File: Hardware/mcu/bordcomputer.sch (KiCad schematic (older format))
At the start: 0 parts

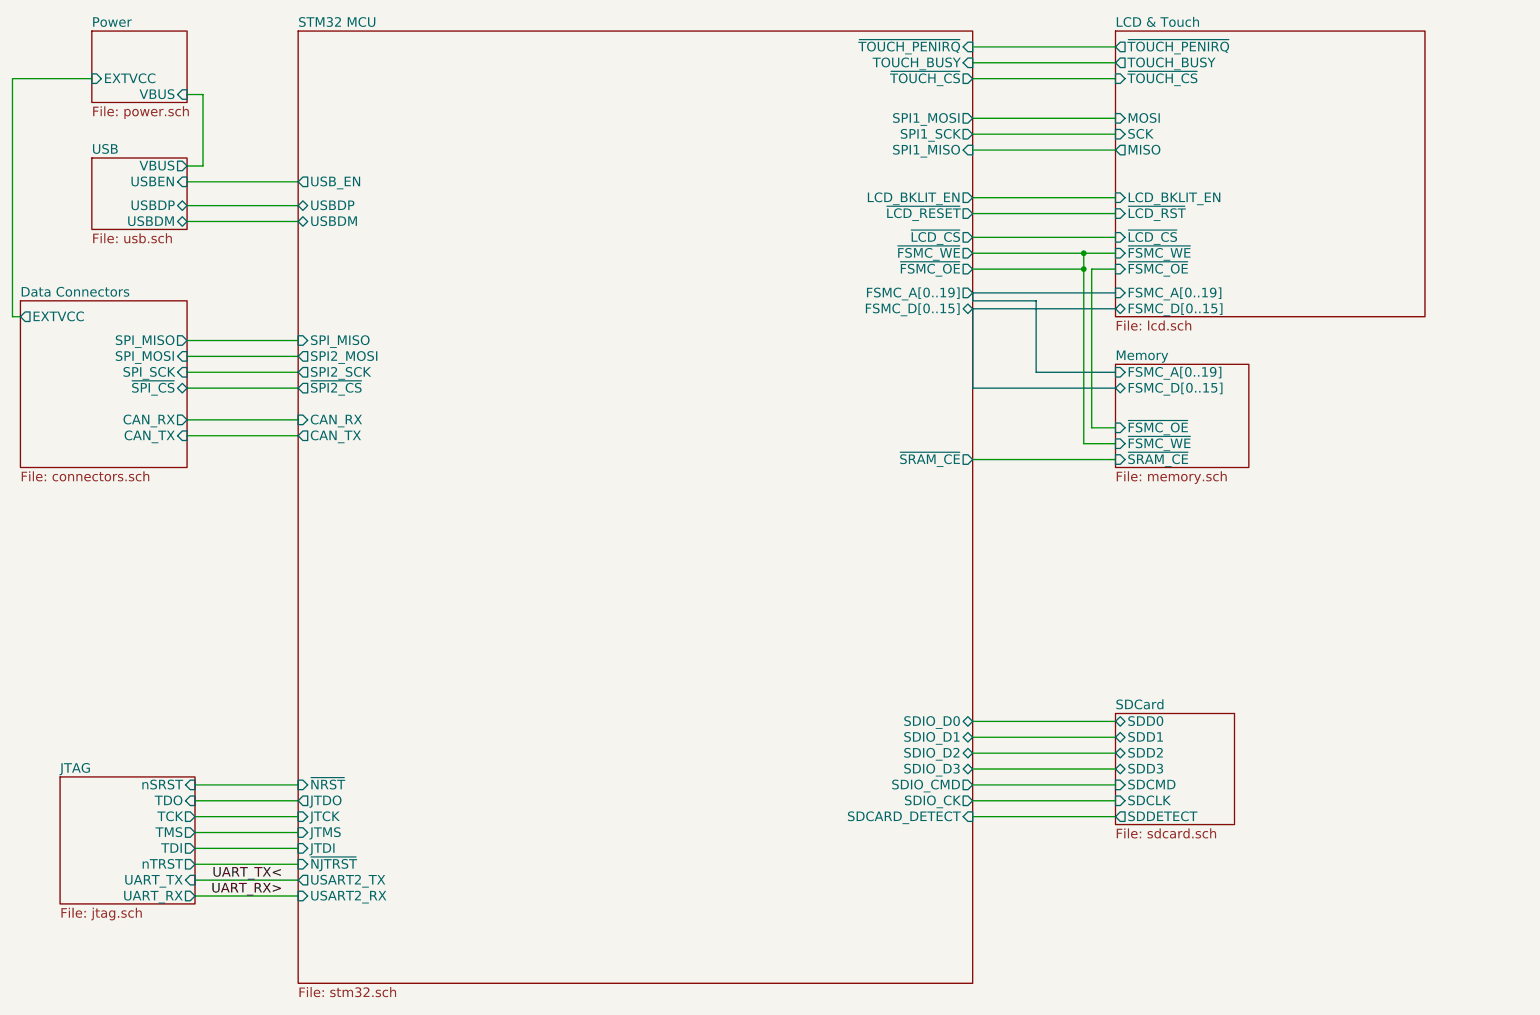
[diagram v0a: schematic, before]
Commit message: splitted schematics are ready. MCU/Display board is ready.
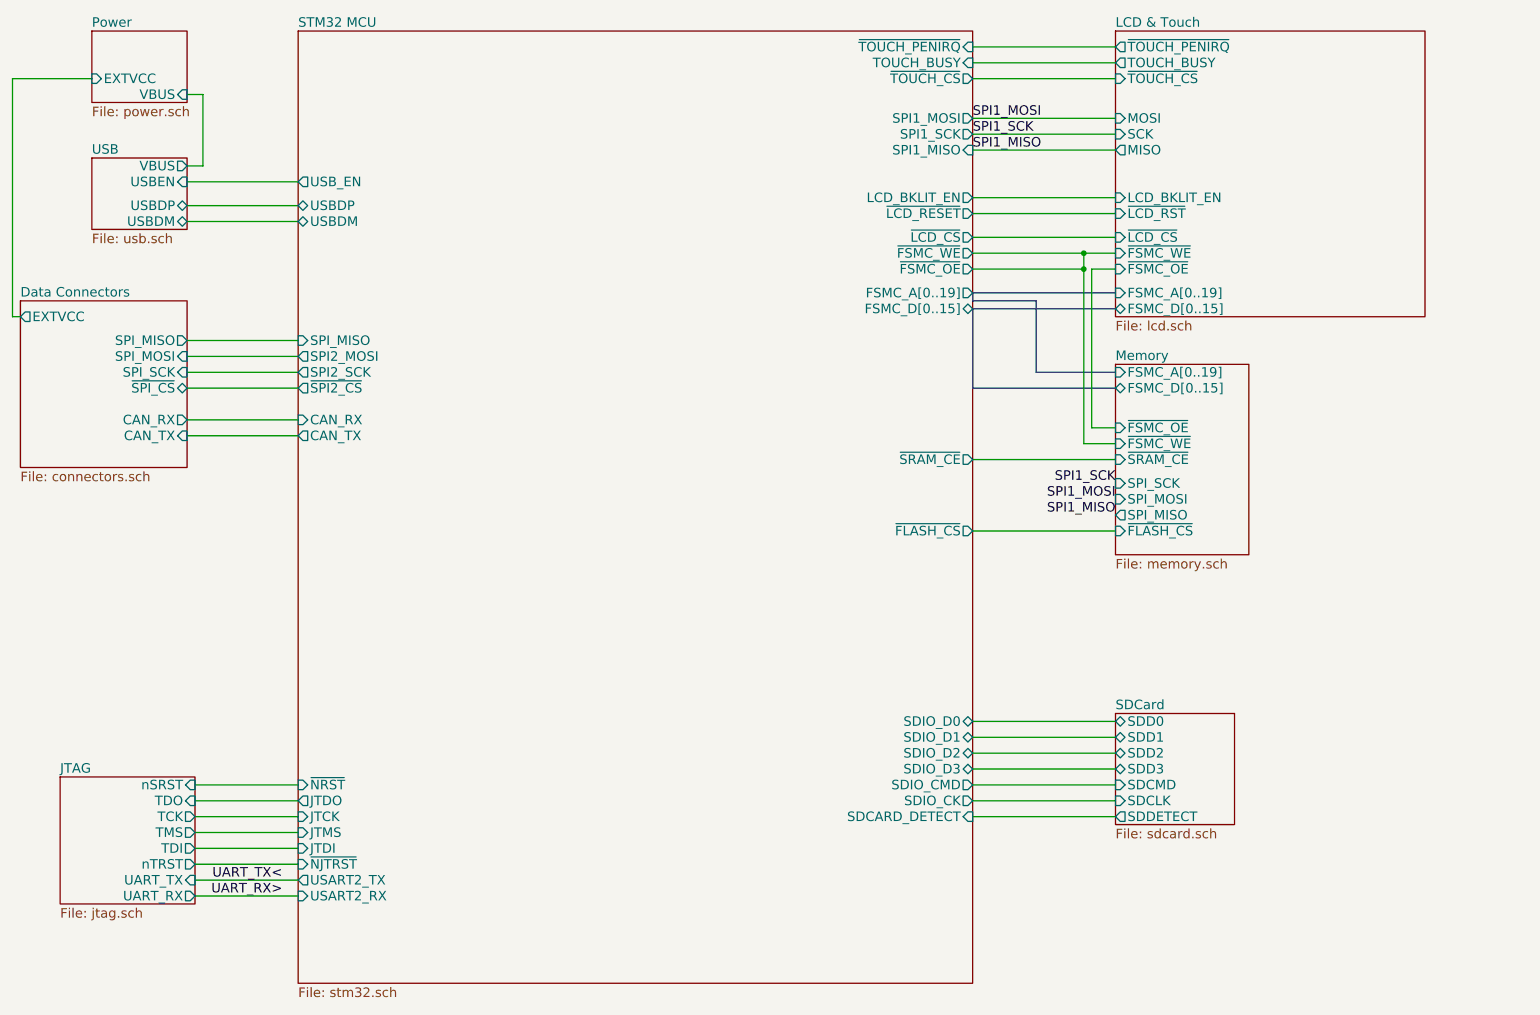
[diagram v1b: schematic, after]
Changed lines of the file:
@@
-EESchema Schematic File Version 2  date Do 10 Mär 2011 01:37:58 CET
+EESchema Schematic File Version 2  date Do 10 Mär 2011 16:44:23 CET
 LIBS:power
 LIBS:device
@@
 EELAYER END
 $Descr A4 11700 8267
+encoding utf-8
 Sheet 1 9
 Title ""
-Date "9 mar 2011"
+Date "10 mar 2011"
 Rev ""
 Comp ""
@@
 $EndDescr
 Wire Wire Line
+	8100 4350 7200 4350
+Wire Wire Line
+	2950 3750 2250 3750
+Wire Wire Line
+	1650 1500 1150 1500
+Wire Wire Line
+	1150 1500 1150 3000
+Wire Wire Line
+	1150 3000 1200 3000
+Wire Bus Line
+	7600 2900 7600 3350
+Wire Bus Line
+	7600 2900 7200 2900
+Wire Bus Line
+	7200 2900 7200 2850
+Wire Bus Line
+	8100 2950 7200 2950
+Wire Bus Line
+	7600 3350 8100 3350
+Wire Wire Line
+	7200 1500 8100 1500
+Wire Wire Line
+	7200 1400 8100 1400
+Wire Wire Line
+	7200 1300 8100 1300
+Wire Wire Line
+	2300 6650 2950 6650
+Wire Wire Line
+	2300 6550 2950 6550
+Wire Wire Line
+	2300 6450 2950 6450
+Wire Wire Line
+	2300 6350 2950 6350
+Wire Wire Line
+	2300 6250 2950 6250
+Wire Wire Line
+	2300 6150 2950 6150
+Wire Wire Line
+	2300 6050 2950 6050
+Wire Wire Line
+	2300 5950 2950 5950
+Wire Wire Line
+	2950 2400 2250 2400
+Wire Wire Line
+	2950 2300 2250 2300
+Wire Wire Line
+	7200 3900 8100 3900
+Connection ~ 7900 2600
+Wire Wire Line
+	7200 2600 8100 2600
+Wire Wire Line
+	8100 3800 7900 3800
+Wire Wire Line
+	7900 3800 7900 2600
+Wire Wire Line
+	2250 2050 2350 2050
+Wire Wire Line
+	2350 2050 2350 1600
+Wire Wire Line
+	2350 1600 2250 1600
+Wire Wire Line
+	8100 2700 7950 2700
+Wire Wire Line
+	7950 2700 7950 3700
+Wire Wire Line
+	7950 3700 8100 3700
+Wire Wire Line
+	7200 2500 8100 2500
+Wire Wire Line
+	7200 2700 7900 2700
+Connection ~ 7900 2700
+Wire Bus Line
+	7200 2850 8100 2850
+Wire Wire Line
+	2250 2150 2950 2150
+Wire Wire Line
+	8100 5550 7200 5550
+Wire Wire Line
+	8100 5650 7200 5650
+Wire Wire Line
+	8100 5750 7200 5750
+Wire Wire Line
+	8100 5850 7200 5850
+Wire Wire Line
+	8100 5950 7200 5950
+Wire Wire Line
+	8100 6050 7200 6050
+Wire Wire Line
+	8100 6150 7200 6150
+Wire Wire Line
+	7200 2250 8100 2250
+Wire Wire Line
+	7200 2350 8100 2350
+Wire Bus Line
+	7200 2950 7200 3450
+Wire Bus Line
+	7200 3450 8100 3450
+Wire Wire Line
+	7200 1750 8100 1750
+Wire Wire Line
+	7200 1850 8100 1850
+Wire Wire Line
+	7200 1950 8100 1950
+Wire Wire Line
+	2250 3650 2950 3650
+Wire Wire Line
+	2250 3150 2950 3150
+Wire Wire Line
+	2250 3250 2950 3250
+Wire Wire Line
+	2250 3350 2950 3350
+Wire Wire Line
 	2250 3450 2950 3450
-Wire Wire Line
-	2250 3350 2950 3350
-Wire Wire Line
-	2250 3250 2950 3250
-Wire Wire Line
-	2250 3150 2950 3150
-Wire Wire Line
-	2250 3650 2950 3650
-Wire Wire Line
-	7200 1950 8100 1950
-Wire Wire Line
-	7200 1850 8100 1850
-Wire Wire Line
-	7200 1750 8100 1750
-Wire Bus Line
-	8100 3450 7200 3450
-Wire Bus Line
-	7200 3450 7200 2950
-Wire Wire Line
-	7200 2350 8100 2350
-Wire Wire Line
-	7200 2250 8100 2250
-Wire Wire Line
-	8100 6150 7200 6150
-Wire Wire Line
-	8100 6050 7200 6050
-Wire Wire Line
-	8100 5950 7200 5950
-Wire Wire Line
-	8100 5850 7200 5850
-Wire Wire Line
-	8100 5750 7200 5750
-Wire Wire Line
-	8100 5650 7200 5650
-Wire Wire Line
-	8100 5550 7200 5550
-Wire Wire Line
-	2250 2150 2950 2150
-Wire Bus Line
-	8100 2850 7200 2850
-Connection ~ 7900 2700
-Wire Wire Line
-	7200 2700 7900 2700
-Wire Wire Line
-	7200 2500 8100 2500
-Wire Wire Line
-	8100 3700 7950 3700
-Wire Wire Line
-	7950 3700 7950 2700
-Wire Wire Line
-	7950 2700 8100 2700
-Wire Wire Line
-	2250 1600 2350 1600
-Wire Wire Line
-	2350 1600 2350 2050
-Wire Wire Line
-	2350 2050 2250 2050
-Wire Wire Line
-	7900 2600 7900 3800
-Wire Wire Line
-	7900 3800 8100 3800
-Wire Wire Line
-	7200 2600 8100 2600
-Connection ~ 7900 2600
-Wire Wire Line
-	7200 3900 8100 3900
-Wire Wire Line
-	2950 2300 2250 2300
-Wire Wire Line
-	2950 2400 2250 2400
-Wire Wire Line
-	2300 5950 2950 5950
-Wire Wire Line
-	2300 6050 2950 6050
-Wire Wire Line
-	2300 6150 2950 6150
-Wire Wire Line
-	2300 6250 2950 6250
-Wire Wire Line
-	2300 6350 2950 6350
-Wire Wire Line
-	2300 6450 2950 6450
-Wire Wire Line
-	2300 6550 2950 6550
-Wire Wire Line
-	2300 6650 2950 6650
-Wire Wire Line
-	7200 1300 8100 1300
-Wire Wire Line
-	7200 1400 8100 1400
-Wire Wire Line
-	7200 1500 8100 1500
-Wire Bus Line
-	8100 3350 7600 3350
-Wire Bus Line
-	7200 2950 8100 2950
-Wire Bus Line
-	7200 2850 7200 2900
-Wire Bus Line
-	7200 2900 7600 2900
-Wire Bus Line
-	7600 2900 7600 3350
-Wire Wire Line
-	1200 3000 1150 3000
-Wire Wire Line
-	1150 3000 1150 1500
-Wire Wire Line
-	1150 1500 1650 1500
-Wire Wire Line
-	2950 3750 2250 3750
+Text Label 8100 4250 2    60   ~ 0
+SPI1_MISO
+Text Label 8100 4150 2    60   ~ 0
+SPI1_MOSI
+Text Label 8100 4050 2    60   ~ 0
+SPI1_SCK
+Text Label 7200 1850 0    60   ~ 0
+SPI1_SCK
+Text Label 7200 1950 0    60   ~ 0
+SPI1_MISO
+Text Label 7200 1750 0    60   ~ 0
+SPI1_MOSI
 $Sheet
 S 1200 2900 1050 1050
@@
 $EndSheet
 $Sheet
-S 8100 3300 840  650
+S 8100 3300 840  1200
 U 4D74466C
 F0 "Memory" 60
@@
 F5 "FSMC_D[0..15]" B L 8100 3450 60
 F6 "FSMC_A[0..19]" I L 8100 3350 60
+F7 "SPI_SCK" I L 8100 4050 60
+F8 "SPI_MOSI" I L 8100 4150 60
+F9 "SPI_MISO" O L 8100 4250 60
+F10 "~FLASH_CS" I L 8100 4350 60
 $EndSheet
 $Sheet
@@
 F38 "SPI2_SCK" O L 2950 3350 60
 F39 "~SPI2_CS" O L 2950 3450 60
+F40 "~FLASH_CS" O R 7200 4350 60
 $EndSheet
 $EndSCHEMATC

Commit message: mounting holes and test version of the bottom of the housing for the sensors pcb
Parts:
- added P101, P102, P103, P104: CONN_1, symbol CONN_1
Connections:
- new net GND: P101.1, P102.1, P103.1, P104.1
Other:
- note added: "Mounting holes"
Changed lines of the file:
@@
-EESchema Schematic File Version 2  date Do 10 Mär 2011 16:44:23 CET
+EESchema Schematic File Version 2  date Mo 21 Mär 2011 03:16:23 CET
 LIBS:power
 LIBS:device
@@
 Sheet 1 9
 Title ""
-Date "10 mar 2011"
+Date "21 mar 2011"
 Rev ""
 Comp ""
@@
 Comment4 ""
 $EndDescr
+Wire Notes Line
+	9850 6500 10550 6500
+Wire Notes Line
+	9850 6500 9850 6950
+Wire Notes Line
+	9850 6950 10550 6950
+Wire Notes Line
+	10550 6950 10550 6500
+Connection ~ 10300 6700
+Wire Wire Line
+	10400 6600 10300 6600
+Wire Wire Line
+	2250 3450 2950 3450
+Wire Wire Line
+	2250 3350 2950 3350
+Wire Wire Line
+	2250 3250 2950 3250
+Wire Wire Line
+	2250 3150 2950 3150
+Wire Wire Line
+	2250 3650 2950 3650
+Wire Wire Line
+	7200 1950 8100 1950
+Wire Wire Line
+	7200 1850 8100 1850
+Wire Wire Line
+	7200 1750 8100 1750
+Wire Bus Line
+	8100 3450 7200 3450
+Wire Bus Line
+	7200 3450 7200 2950
+Wire Wire Line
+	7200 2350 8100 2350
+Wire Wire Line
+	7200 2250 8100 2250
+Wire Wire Line
+	8100 6150 7200 6150
+Wire Wire Line
+	8100 6050 7200 6050
+Wire Wire Line
+	8100 5950 7200 5950
+Wire Wire Line
+	8100 5850 7200 5850
+Wire Wire Line
+	8100 5750 7200 5750
+Wire Wire Line
+	8100 5650 7200 5650
+Wire Wire Line
+	8100 5550 7200 5550
+Wire Wire Line
+	2250 2150 2950 2150
+Wire Bus Line
+	8100 2850 7200 2850
+Connection ~ 7900 2700
+Wire Wire Line
+	7200 2700 7900 2700
+Wire Wire Line
+	7200 2500 8100 2500
+Wire Wire Line
+	8100 3700 7950 3700
+Wire Wire Line
+	7950 3700 7950 2700
+Wire Wire Line
+	7950 2700 8100 2700
+Wire Wire Line
+	2250 1600 2350 1600
+Wire Wire Line
+	2350 1600 2350 2050
+Wire Wire Line
+	2350 2050 2250 2050
+Wire Wire Line
+	7900 2600 7900 3800
+Wire Wire Line
+	7900 3800 8100 3800
+Wire Wire Line
+	7200 2600 8100 2600
+Connection ~ 7900 2600
+Wire Wire Line
+	7200 3900 8100 3900
+Wire Wire Line
+	2950 2300 2250 2300
+Wire Wire Line
+	2950 2400 2250 2400
+Wire Wire Line
+	2300 5950 2950 5950
+Wire Wire Line
+	2300 6050 2950 6050
+Wire Wire Line
+	2300 6150 2950 6150
+Wire Wire Line
+	2300 6250 2950 6250
+Wire Wire Line
+	2300 6350 2950 6350
+Wire Wire Line
+	2300 6450 2950 6450
+Wire Wire Line
+	2300 6550 2950 6550
+Wire Wire Line
+	2300 6650 2950 6650
+Wire Wire Line
+	7200 1300 8100 1300
+Wire Wire Line
+	7200 1400 8100 1400
+Wire Wire Line
+	7200 1500 8100 1500
+Wire Bus Line
+	8100 3350 7600 3350
+Wire Bus Line
+	7200 2950 8100 2950
+Wire Bus Line
+	7200 2850 7200 2900
+Wire Bus Line
+	7200 2900 7600 2900
+Wire Bus Line
+	7600 2900 7600 3350
+Wire Wire Line
+	1200 3000 1150 3000
+Wire Wire Line
+	1150 3000 1150 1500
+Wire Wire Line
+	1150 1500 1650 1500
+Wire Wire Line
+	2950 3750 2250 3750
 Wire Wire Line
 	8100 4350 7200 4350
 Wire Wire Line
-	2950 3750 2250 3750
-Wire Wire Line
-	1650 1500 1150 1500
-Wire Wire Line
-	1150 1500 1150 3000
-Wire Wire Line
-	1150 3000 1200 3000
-Wire Bus Line
-	7600 2900 7600 3350
-Wire Bus Line
-	7600 2900 7200 2900
-Wire Bus Line
-	7200 2900 7200 2850
-Wire Bus Line
-	8100 2950 7200 2950
-Wire Bus Line
-	7600 3350 8100 3350
-Wire Wire Line
-	7200 1500 8100 1500
-Wire Wire Line
-	7200 1400 8100 1400
-Wire Wire Line
-	7200 1300 8100 1300
-Wire Wire Line
-	2300 6650 2950 6650
-Wire Wire Line
-	2300 6550 2950 6550
-Wire Wire Line
-	2300 6450 2950 6450
-Wire Wire Line
-	2300 6350 2950 6350
-Wire Wire Line
-	2300 6250 2950 6250
-Wire Wire Line
-	2300 6150 2950 6150
-Wire Wire Line
-	2300 6050 2950 6050
-Wire Wire Line
-	2300 5950 2950 5950
-Wire Wire Line
-	2950 2400 2250 2400
-Wire Wire Line
-	2950 2300 2250 2300
-Wire Wire Line
-	7200 3900 8100 3900
-Connection ~ 7900 2600
-Wire Wire Line
-	7200 2600 8100 2600
-Wire Wire Line
-	8100 3800 7900 3800
-Wire Wire Line
-	7900 3800 7900 2600
-Wire Wire Line
-	2250 2050 2350 2050
-Wire Wire Line
-	2350 2050 2350 1600
-Wire Wire Line
-	2350 1600 2250 1600
-Wire Wire Line
-	8100 2700 7950 2700
-Wire Wire Line
-	7950 2700 7950 3700
-Wire Wire Line
-	7950 3700 8100 3700
-Wire Wire Line
-	7200 2500 8100 2500
-Wire Wire Line
-	7200 2700 7900 2700
-Connection ~ 7900 2700
-Wire Bus Line
-	7200 2850 8100 2850
-Wire Wire Line
-	2250 2150 2950 2150
-Wire Wire Line
-	8100 5550 7200 5550
-Wire Wire Line
-	8100 5650 7200 5650
-Wire Wire Line
-	8100 5750 7200 5750
-Wire Wire Line
-	8100 5850 7200 5850
-Wire Wire Line
-	8100 5950 7200 5950
-Wire Wire Line
-	8100 6050 7200 6050
-Wire Wire Line
-	8100 6150 7200 6150
-Wire Wire Line
-	7200 2250 8100 2250
-Wire Wire Line
-	7200 2350 8100 2350
-Wire Bus Line
-	7200 2950 7200 3450
-Wire Bus Line
-	7200 3450 8100 3450
-Wire Wire Line
-	7200 1750 8100 1750
-Wire Wire Line
-	7200 1850 8100 1850
-Wire Wire Line
-	7200 1950 8100 1950
-Wire Wire Line
-	2250 3650 2950 3650
-Wire Wire Line
-	2250 3150 2950 3150
-Wire Wire Line
-	2250 3250 2950 3250
-Wire Wire Line
-	2250 3350 2950 3350
-Wire Wire Line
-	2250 3450 2950 3450
+	10300 6600 10300 6900
+Connection ~ 10300 6800
+$Comp
+L GND #PWR01
+U 1 1 4D86B163
+P 10400 6600
+F 0 "#PWR01" H 10400 6600 30  0001 C CNN
+F 1 "GND" H 10400 6530 30  0001 C CNN
+	1    10400 6600
+	0    -1   -1   0
+$EndComp
+$Comp
+L CONN_1 P104
+U 1 1 4D86B15F
+P 10150 6900
+F 0 "P104" H 10230 6900 40  0000 L CNN
+F 1 "CONN_1" H 10150 6955 30  0001 C CNN
+	1    10150 6900
+	-1   0    0    1
+$EndComp
+$Comp
+L CONN_1 P103
+U 1 1 4D86B15C
+P 10150 6800
+F 0 "P103" H 10230 6800 40  0000 L CNN
+F 1 "CONN_1" H 10150 6855 30  0001 C CNN
+	1    10150 6800
+	-1   0    0    1
+$EndComp
+$Comp
+L CONN_1 P102
+U 1 1 4D86B15A
+P 10150 6700
+F 0 "P102" H 10230 6700 40  0000 L CNN
+F 1 "CONN_1" H 10150 6755 30  0001 C CNN
+	1    10150 6700
+	-1   0    0    1
+$EndComp
+$Comp
+L CONN_1 P101
+U 1 1 4D86B156
+P 10150 6600
+F 0 "P101" H 10230 6600 40  0000 L CNN
+F 1 "CONN_1" H 10150 6655 30  0001 C CNN
+	1    10150 6600
+	-1   0    0    1
+$EndComp
+Text Notes 9850 6500 0    60   ~ 0
+Mounting holes
 Text Label 8100 4250 2    60   ~ 0
 SPI1_MISO
